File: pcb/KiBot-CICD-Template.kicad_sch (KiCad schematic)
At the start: 0 parts

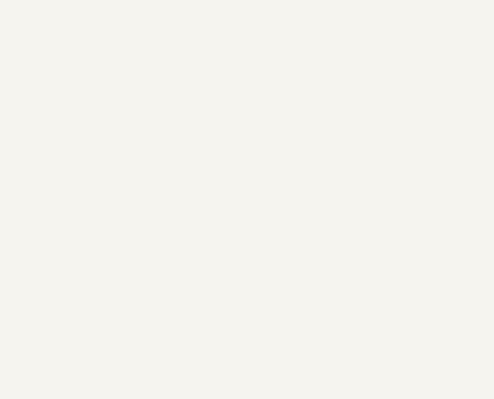
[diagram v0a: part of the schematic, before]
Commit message: rework kibot to inherite from single file
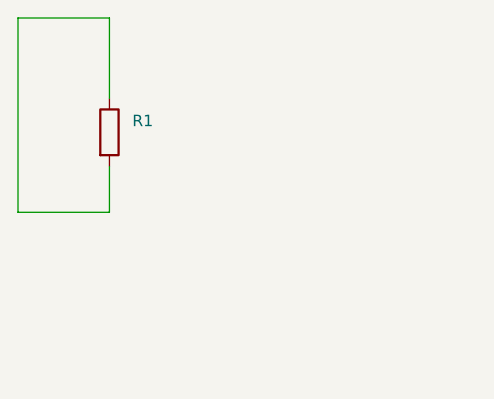
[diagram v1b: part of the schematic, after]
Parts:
- added R1: (no value), symbol Device:R
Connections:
- new net: R1.1, R1.2
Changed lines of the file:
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@@
     (comment 4 "CERN Open Hardware Licence v2.0")
+  )
+  (wire (pts (xy 99.06 97.79) (xy 99.06 119.38))
+    (stroke (width 0) (type default) (color 0 0 0 0))
+  )
+  (wire (pts (xy 99.06 119.38) (xy 109.22 119.38))
+    (stroke (width 0) (type default) (color 0 0 0 0))
+  )
+  (wire (pts (xy 109.22 106.68) (xy 109.22 97.79))
+    (stroke (width 0) (type default) (color 0 0 0 0))
+  )
+  (wire (pts (xy 109.22 97.79) (xy 99.06 97.79))
+    (stroke (width 0) (type default) (color 0 0 0 0))
+  )
+  (wire (pts (xy 109.22 119.38) (xy 109.22 114.3))
+    (stroke (width 0) (type default) (color 0 0 0 0))
   )
   (symbol (lib_id "Graphic:Logo_Open_Hardware_Small") (at 274.32 175.26 0) (unit 1)
@@
     )
   )
+  (symbol (lib_id "Device:R") (at 109.22 110.49 0) (unit 1)
+    (in_bom yes) (on_board yes) (fields_autoplaced)
+    (property "Reference" "R1" (id 0) (at 111.76 109.2199 0)
+      (effects (font (size 1.27 1.27)) (justify left))
+    )
+    (property "Value" "" (id 1) (at 111.76 111.7599 0)
+      (effects (font (size 1.27 1.27)) (justify left))
+    )
+    (property "Footprint" "" (id 2) (at 107.442 110.49 90)
+      (effects (font (size 1.27 1.27)) hide)
+    )
+    (property "Datasheet" "~" (id 3) (at 109.22 110.49 0)
+      (effects (font (size 1.27 1.27)) hide)
+    )
+    (property "Variant" "DNP" (id 4) (at 109.22 110.49 0)
+      (effects (font (size 1.27 1.27)) hide)
+    )
+    (pin "1")
+    (pin "2")
+  )
   (sheet_instances
     (path "/" (page "1"))
@@
       (reference "#LOGO1") (unit 1) (value "Logo_Open_Hardware_Small") (footprint "Symbol:OSHW-Symbol_6.7x6mm_SilkScreen")
     )
+    (path "/5f38bdb2-3657-474e-8e86-d6bb0b298110"
+      (reference "R1") (unit 1) (value "R") (footprint "")
+    )
   )
